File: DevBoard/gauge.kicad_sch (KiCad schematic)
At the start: 78 parts, among them J101 Pack (welded 4S) - use instea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, J102 Cell 1 NTC 10k 103AT, J103 EV2400 SMBus, J104 Bench PACK_P, J105 Cell 2 NTC 10k 103AT, J106 Cell 3 NTC 10k 103AT, J107 Cell 4 NTC 10k 103AT, Q101 AGM404AP1, Q102 AGM404AP1, Q103 BSS138, Q104 AO3400A, SW101 WAKE, U101 BQ40Z50RSMR-R2, U102 BQ294700DSGR

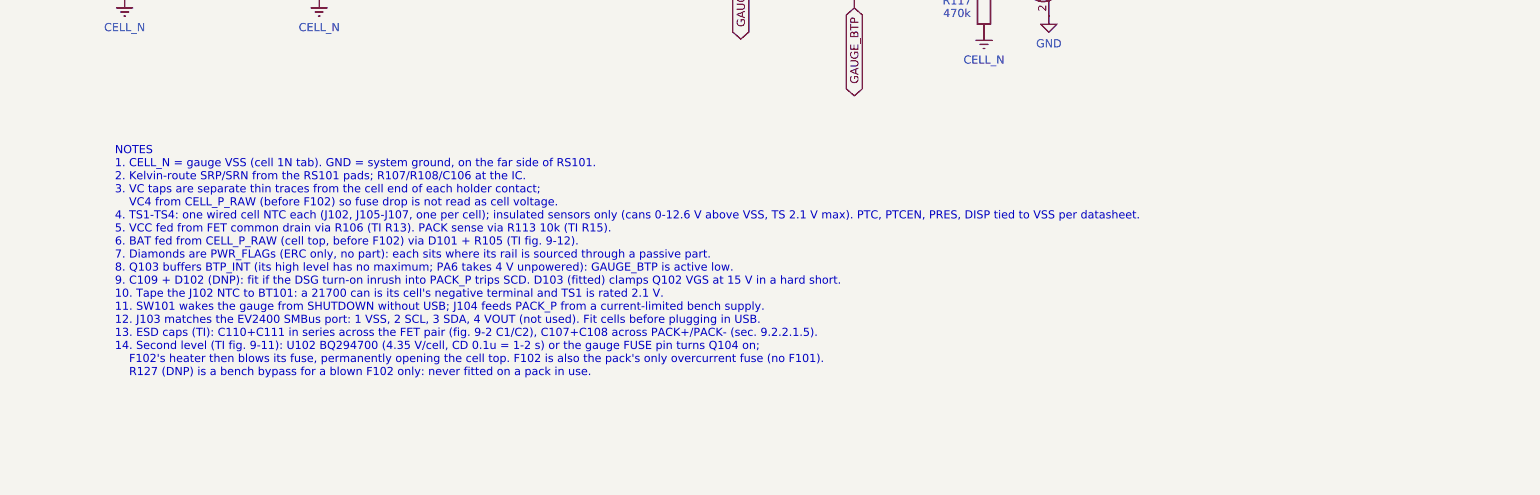
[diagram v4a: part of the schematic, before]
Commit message: Dev board: USB-C liquid detection, schematic review 3 fixes, new datasheets
Liquid detection (TPS25751 datasheet 9.2.2.2, both ports): TPD2S300 U405/U505
on SBU1/SBU2 into GPIO4/5, switched 100k pull-up / 1M pull-down (Q403-Q406)
on GPIO6/7. R440/R540 short D+/D- (passive BC1.2 DCP); D403/D503 removed.

Schematic review 3 (docs/devboard/schematic-review-3-2026-10-14.md):
- H1: TPD2S300 FLT -> GPIO3 fault input (SBU_FLT, R441 pull-up), as on
  TI's TPS25751EVM, so a VBUS-SBU short turns VBUS off.
- H2: R442/R443 hold the liquid-detect FETs off while GPIO6/7 are Hi-Z.
- H3: BQ25756 tuning parts from the EVM: 0R in gate and BTST lines
  (R444-R449), DNP RC snubbers on SW1/SW2 (R450/C454, R451/C455).
- H4: MonolithDev:TPS25751D, stock symbol with GPIO11 bidirectional;
  ERC now 0 errors, 8 expected GPIO-to-GND warnings.
- Gauge data flash and handling rules (Min Blow Fuse Voltage 10.5 V,
  COV Delay 1 s, no cell hot-swap with power on) in the bring-up
  checklist and gauge sheet note 15.
- Docs: A6 revision log, power budget, circuit description, README
  items 16/34/35/36.

Datasheets and app notes added (sources.csv): BQ2947, WSFB1514, TPD2S300,
BQ40Z50-R2 TRM, SLUA660, BQ25756 and TPS25751 EVM guides, discretes.

Co-Authored-By: Claude Opus 5.5 <noreply@anthropic.com>
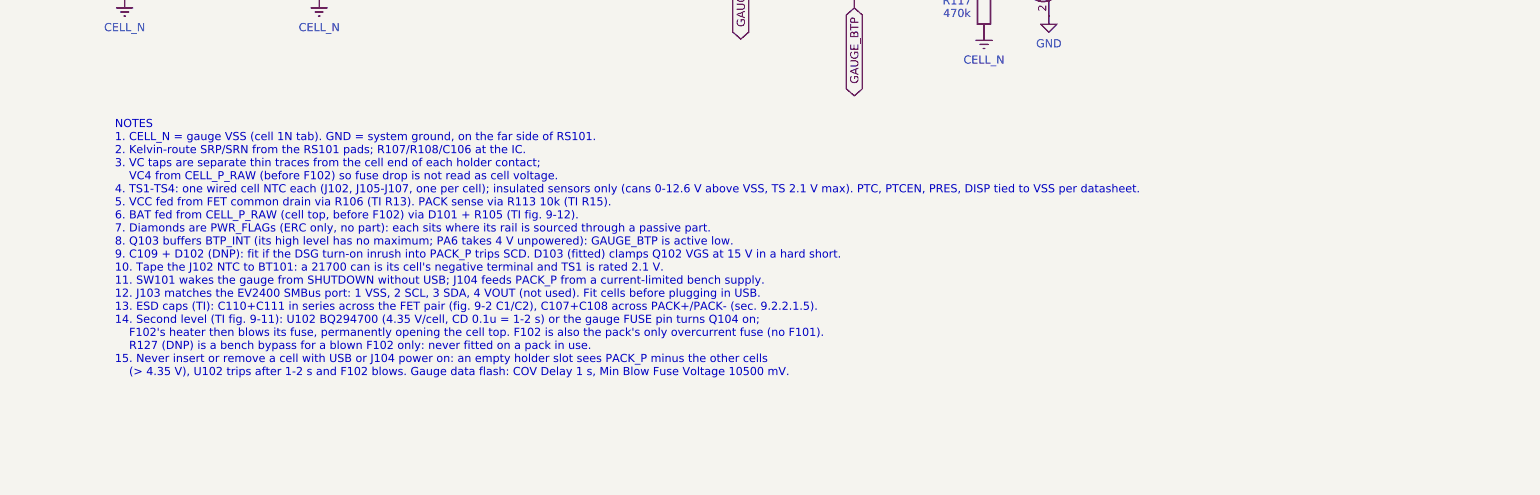
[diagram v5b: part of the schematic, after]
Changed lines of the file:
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@@
 		)
 	)
-	(text "NOTES\n1. CELL_N = gauge VSS (cell 1N tab). GND = system ground, on the far side of RS101.\n2. Kelvin-route SRP/SRN from the RS101 pads; R107/R108/C106 at the IC.\n3. VC taps are separate thin traces from the cell end of each holder contact;\n    VC4 from CELL_P_RAW (before F102) so fuse drop is not read as cell voltage.\n4. TS1-TS4: one wired cell NTC each (J102, J105-J107, one per cell); insulated sensors only (cans 0-12.6 V above VSS, TS 2.1 V max). PTC, PTCEN, PRES, DISP tied to VSS per datasheet.\n5. VCC fed from FET common drain via R106 (TI R13). PACK sense via R113 10k (TI R15).\n6. BAT fed from CELL_P_RAW (cell top, before F102) via D101 + R105 (TI fig. 9-12).\n7. Diamonds are PWR_FLAGs (ERC only, no part): each sits where its rail is sourced through a passive part.\n8. Q103 buffers BTP_INT (its high level has no maximum; PA6 takes 4 V unpowered): GAUGE_BTP is active low.\n9. C109 + D102 (DNP): fit if the DSG turn-on inrush into PACK_P trips SCD. D103 (fitted) clamps Q102 VGS at 15 V in a hard short.\n10. Tape the J102 NTC to BT101: a 21700 can is its cell's negative terminal and TS1 is rated 2.1 V.\n11. SW101 wakes the gauge from SHUTDOWN without USB; J104 feeds PACK_P from a current-limited bench supply.\n12. J103 matches the EV2400 SMBus port: 1 VSS, 2 SCL, 3 SDA, 4 VOUT (not used). Fit cells before plugging in USB.\n13. ESD caps (TI): C110+C111 in series across the FET pair (fig. 9-2 C1/C2), C107+C108 across PACK+/PACK- (sec. 9.2.2.1.5).\n14. Second level (TI fig. 9-11): U102 BQ294700 (4.35 V/cell, CD 0.1u = 1-2 s) or the gauge FUSE pin turns Q104 on;\n    F102's heater then blows its fuse, permanently opening the cell top. F102 is also the pack's only overcurrent fuse (no F101).\n    R127 (DNP) is a bench bypass for a blown F102 only: never fitted on a pack in use."
+	(text "NOTES\n1. CELL_N = gauge VSS (cell 1N tab). GND = system ground, on the far side of RS101.\n2. Kelvin-route SRP/SRN from the RS101 pads; R107/R108/C106 at the IC.\n3. VC taps are separate thin traces from the cell end of each holder contact;\n    VC4 from CELL_P_RAW (before F102) so fuse drop is not read as cell voltage.\n4. TS1-TS4: one wired cell NTC each (J102, J105-J107, one per cell); insulated sensors only (cans 0-12.6 V above VSS, TS 2.1 V max). PTC, PTCEN, PRES, DISP tied to VSS per datasheet.\n5. VCC fed from FET common drain via R106 (TI R13). PACK sense via R113 10k (TI R15).\n6. BAT fed from CELL_P_RAW (cell top, before F102) via D101 + R105 (TI fig. 9-12).\n7. Diamonds are PWR_FLAGs (ERC only, no part): each sits where its rail is sourced through a passive part.\n8. Q103 buffers BTP_INT (its high level has no maximum; PA6 takes 4 V unpowered): GAUGE_BTP is active low.\n9. C109 + D102 (DNP): fit if the DSG turn-on inrush into PACK_P trips SCD. D103 (fitted) clamps Q102 VGS at 15 V in a hard short.\n10. Tape the J102 NTC to BT101: a 21700 can is its cell's negative terminal and TS1 is rated 2.1 V.\n11. SW101 wakes the gauge from SHUTDOWN without USB; J104 feeds PACK_P from a current-limited bench supply.\n12. J103 matches the EV2400 SMBus port: 1 VSS, 2 SCL, 3 SDA, 4 VOUT (not used). Fit cells before plugging in USB.\n13. ESD caps (TI): C110+C111 in series across the FET pair (fig. 9-2 C1/C2), C107+C108 across PACK+/PACK- (sec. 9.2.2.1.5).\n14. Second level (TI fig. 9-11): U102 BQ294700 (4.35 V/cell, CD 0.1u = 1-2 s) or the gauge FUSE pin turns Q104 on;\n    F102's heater then blows its fuse, permanently opening the cell top. F102 is also the pack's only overcurrent fuse (no F101).\n    R127 (DNP) is a bench bypass for a blown F102 only: never fitted on a pack in use.\n15. Never insert or remove a cell with USB or J104 power on: an empty holder slot sees PACK_P minus the other cells\n    (> 4.35 V), U102 trips after 1-2 s and F102 blows. Gauge data flash: COV Delay 1 s, Min Blow Fuse Voltage 10500 mV."
 		(exclude_from_sim no)
 		(at 196.596 248.412 0)

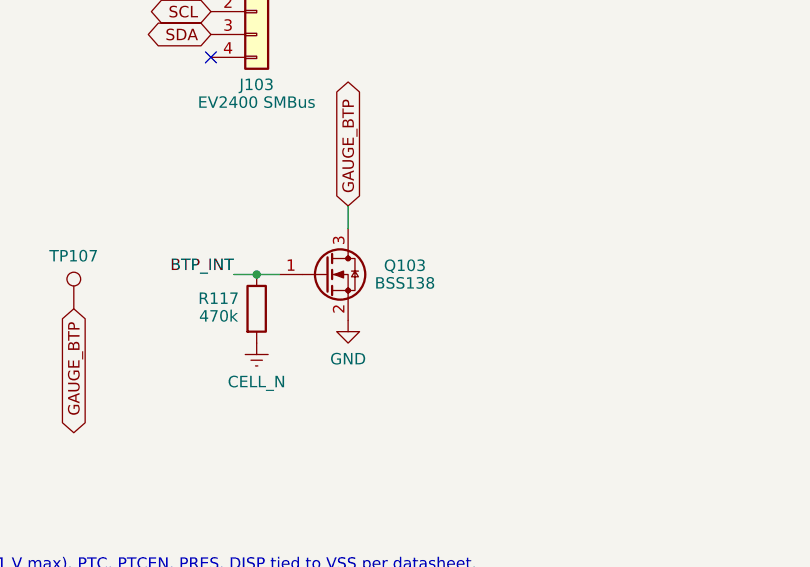
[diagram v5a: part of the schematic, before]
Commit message: Dev board: cost-down pass (about $113 -> $80 per board at 5 boards)
Swaps from docs/devboard/cost-down-2026-10-14.md, datasheet-checked:
- L401/L501 XAL7030 -> SMMS1040-2R2M (Isat 18 A, Irms 12 A, 9 mOhm)
- L402/L502 SRP5030T -> APS0530M3R3H (new footprint L_Coilank_APS0530)
- L201 SRN4018TA -> FNR4030S100MT
- U203 TPS70950 -> HT7550-1, C204/C205 10 uF per Holtek's basic circuit
- C431/C434/C435 47 uF 1210 -> 22 uF 1206 (bank ~114 uF effective)
- JLC basic/preferred equivalents: D103, D401, R410/R412, C105/C206,
  C406, Q103 -> AO3400A
- D301 (out of stock) -> red KT-0603R
- R431/R531 -> bridged solder jumper
- 34 test loops -> bare pads; pin headers hand-soldered
- U301 bought from ST and consigned to JLC

ERC unchanged (0 errors, 8 expected GPIO-to-GND warnings).

Co-Authored-By: Claude Opus 5.5 <noreply@anthropic.com>
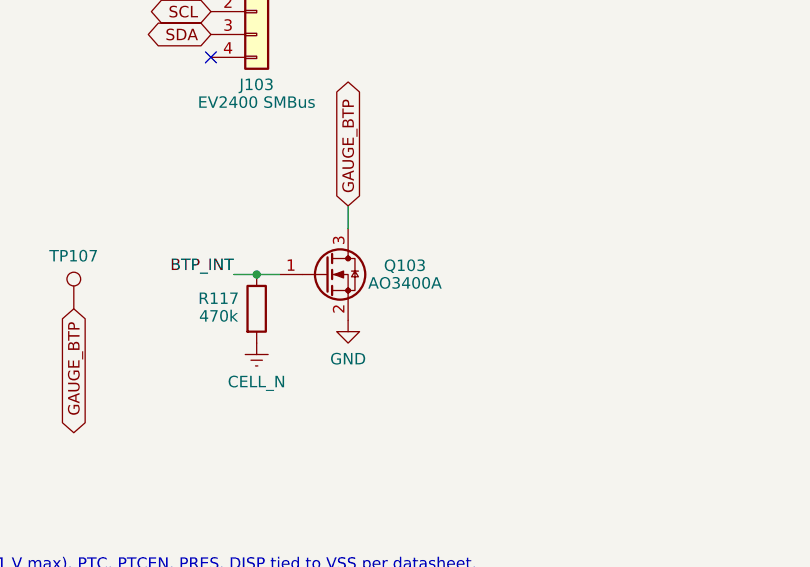
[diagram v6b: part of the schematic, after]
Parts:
- C105: footprint Capacitor_SMD:C_0805_2012Metric -> Capacitor_SMD:C_1206_3216Metric; LCSC C2762602 -> C50254; MPN CL21B225KBYNNNE -> CL31B225KBHNNNE; Notes PBI sits near VBAT (16.8 V): 50 V X7R 0805 keeps most of it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 -> PBI sits near VBAT (16.8 V): 50 V X7R 1206 keeps more of it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
- D103: LCSC C173427 -> C19077412; MPN BZT52C15 -> BZT52C15 (JLC preferred C19077412)
- J102, J104, J105, J106, J107: LCSC C492401 -> (none); Sourcing (none) -> Hand-solder, not JLC assembled (through-hole; LCSC C492401 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
- J103: LCSC C2691448 -> (none); Sourcing (none) -> Hand-solder, not JLC assembled (through-hole; LCSC C2691448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
- Q103: value BSS138 -> AO3400A; LCSC C52895 -> C20917; MPN BSS138 (onsemi) -> AO3400A (AOS); Notes BTP_INT level shift (inverts: GAUGE_BTP active low). BSS138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 -> BTP_INT level shift (inverts: GAUGE_BTP active low). AO3400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
- TP101, TP102, TP103, TP104, TP105, TP106, TP107, TP108: footprint MonolithDev:TestPoint_Harwin_S2761_0603 -> TestPoint:TestPoint_Pad_D1.5mm; LCSC C55121754 -> (none); MPN RH-S2761-46R (ronghe; Harwin S2761-46R equivalent) -> (none); now left out of the parts list

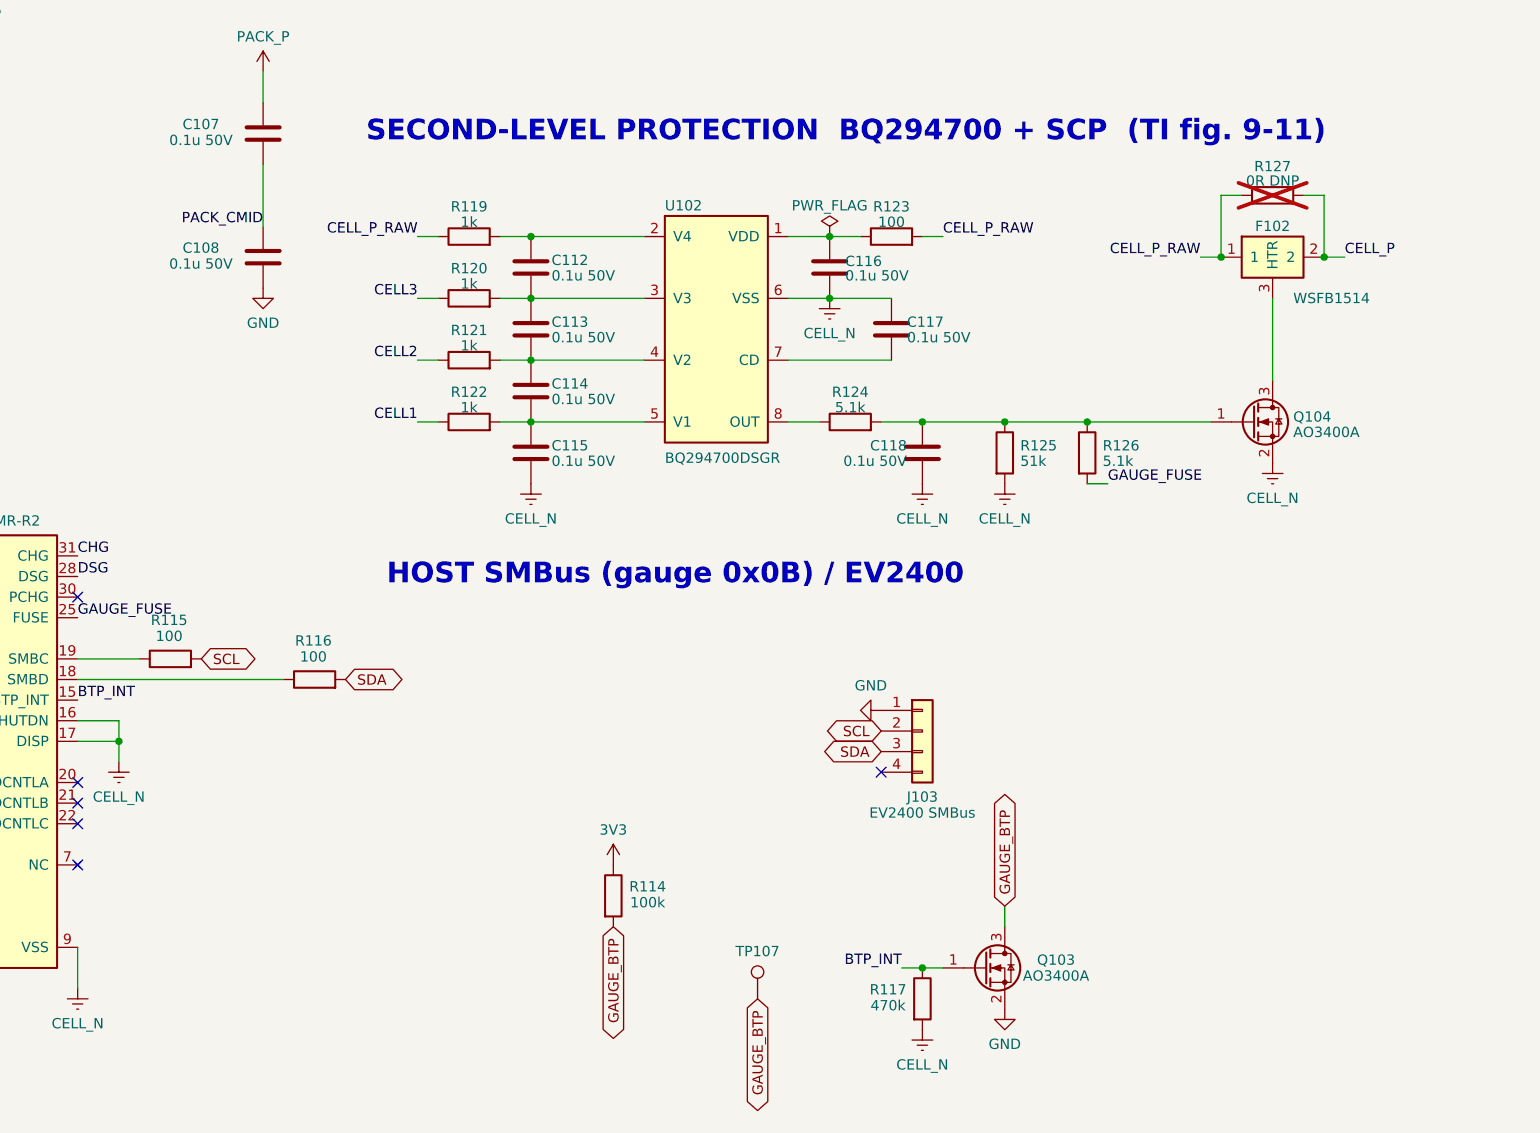
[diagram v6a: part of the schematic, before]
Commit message: Dev board: reset the layout to parts + outline, sync board to schematic
tools/reset_board.py strips every track (659), via (685), zone (79, incl.
the antenna keep-out), board silkscreen text (50) and group from the
board, deletes the 11 parts no longer in the schematic (F101, D403/D503,
R405-R408, R505-R508), reloads the 61 parts whose footprint changed at
their old positions, and stages the 75 new parts below the outline.
netlist_to_board.py then set nets and fields: 0 schematic parity issues.

Schematic: field placement re-run on gauge and port sheets (0 text
overlaps, netlist unchanged); SBU_FLT stub shortened. place_parts.py
points at F102. README layout status and rev2 notes updated, including
the TPD2S300 0.4 mm escape decision.

Co-Authored-By: Claude Opus 5.5 <noreply@anthropic.com>
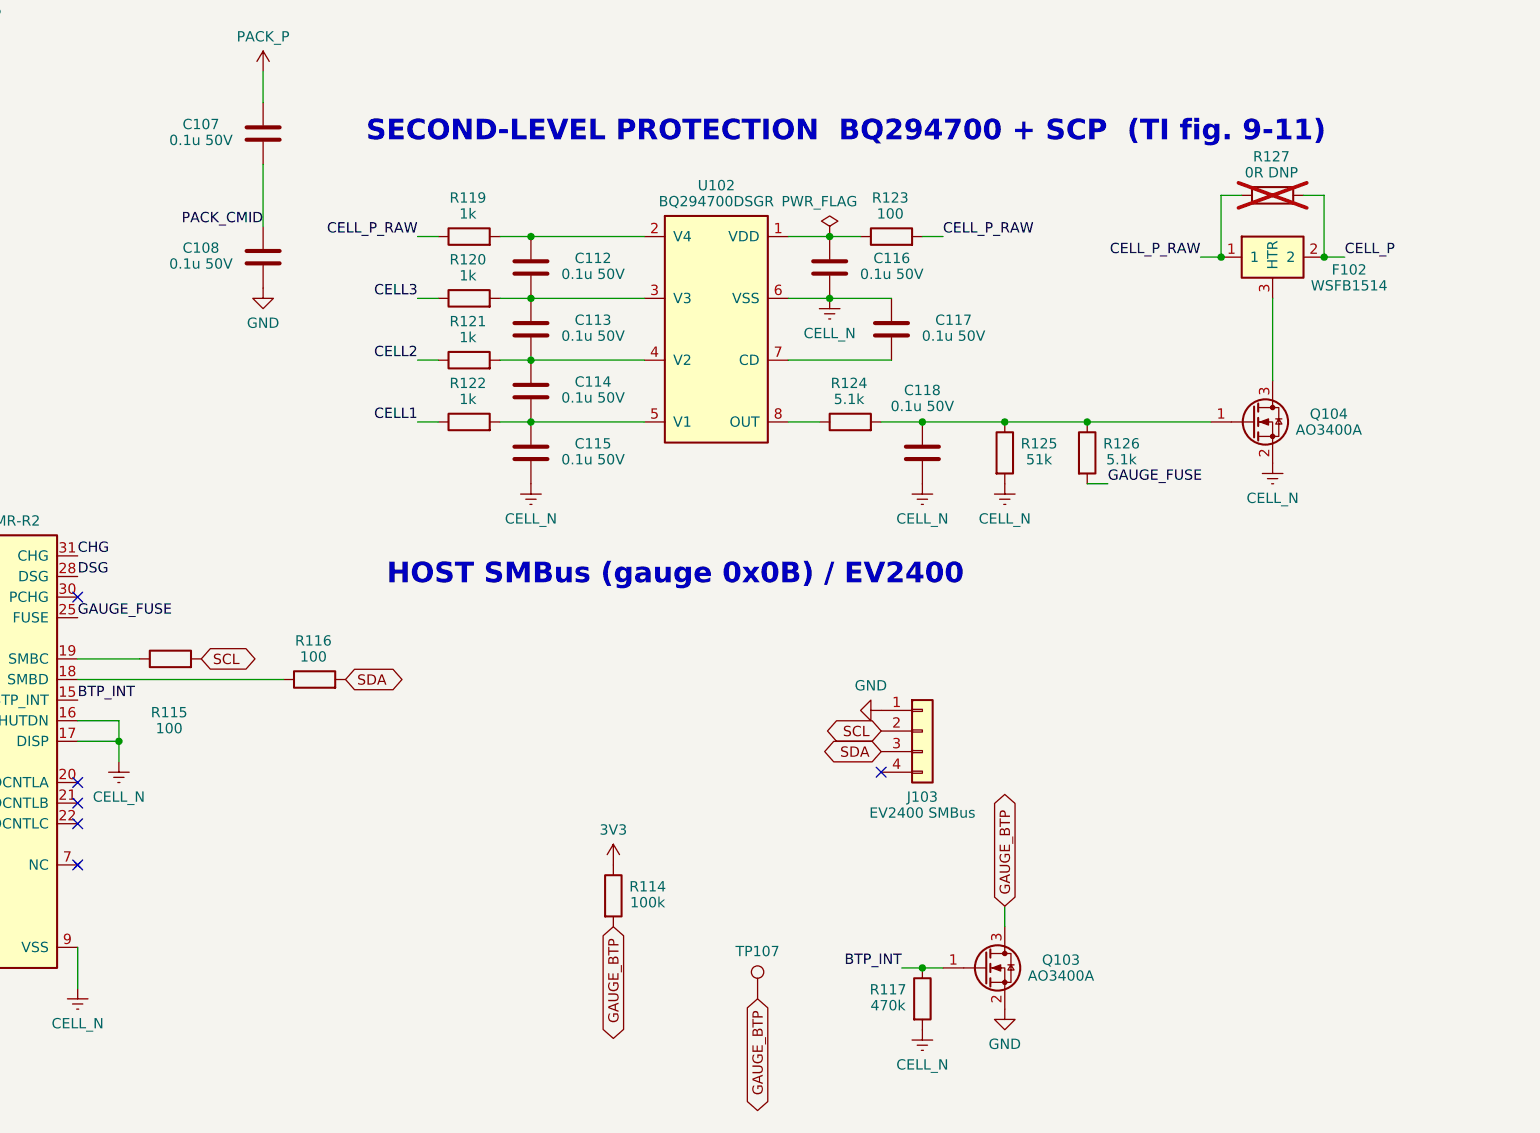
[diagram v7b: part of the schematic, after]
